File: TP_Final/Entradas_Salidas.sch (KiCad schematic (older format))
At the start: 89 parts, among them J109 BG2, J110 BG2, J111 BG2, J112 Conector pol. 1x3, J113 BG2, J114 Conector pol. 1x3, J115 Conector pol. 1x3, J116 BG2, J117 BG2, Q108 2N3904, Q109 2N3904, Q110 2N3904, U104 OP07, U105 OP07, U106 OP07, U107 LM7805_TO220, U108 LD1117S33TR_SOT223

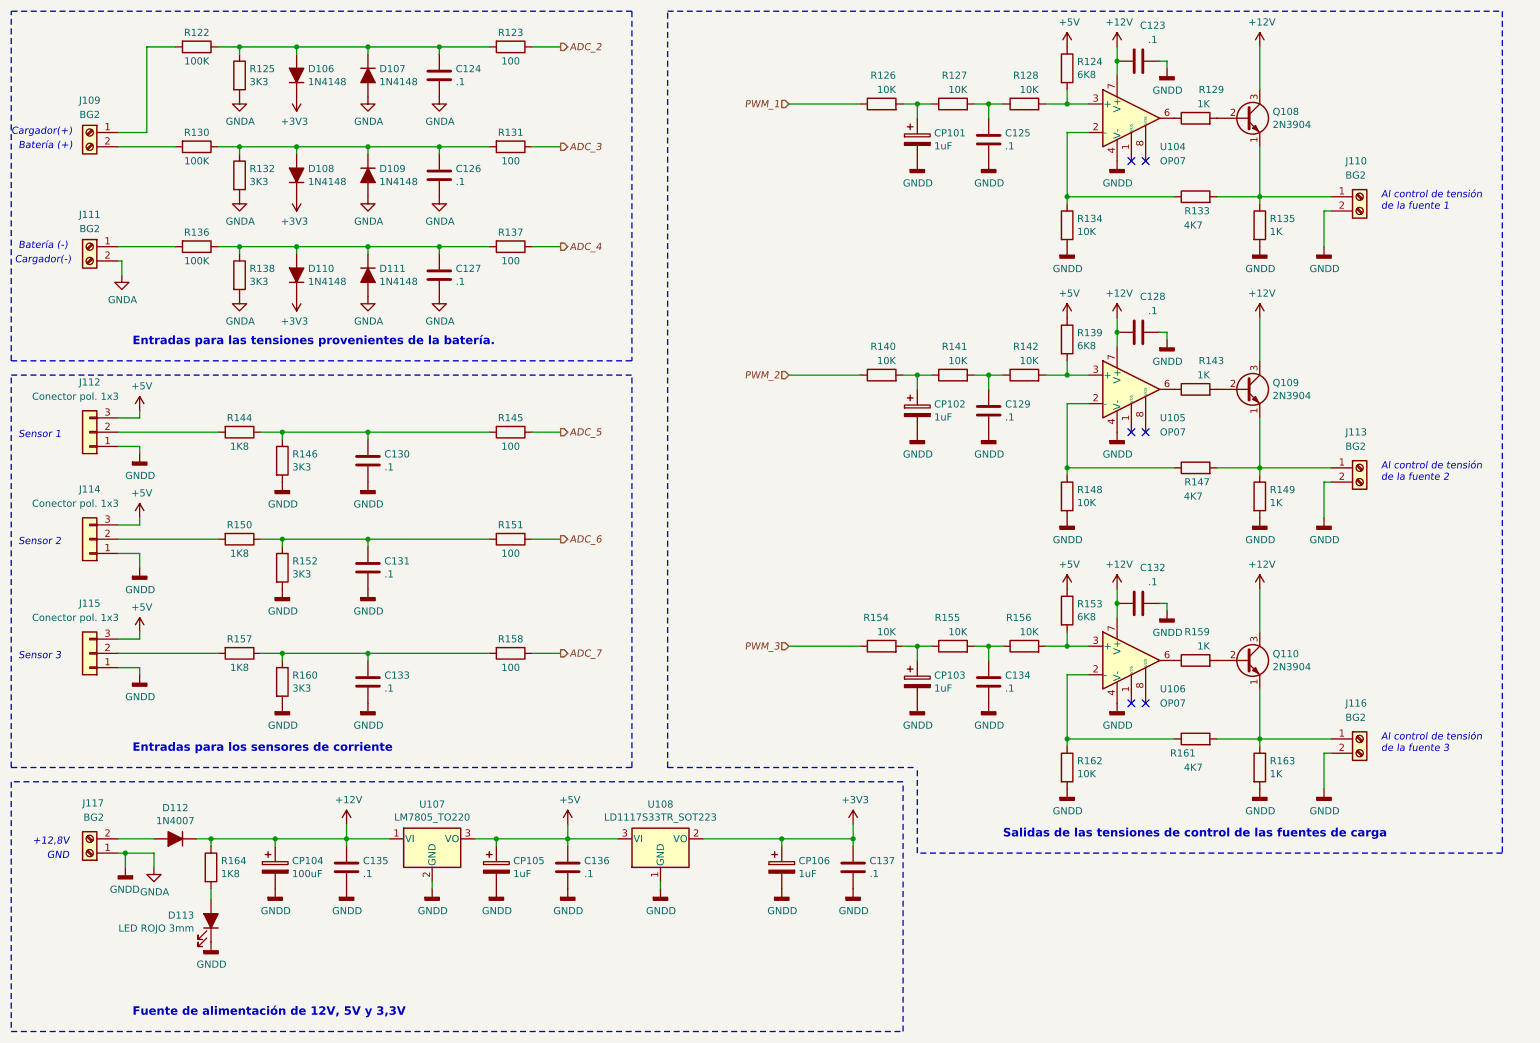
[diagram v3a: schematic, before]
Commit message: Agrego agujeros de montaje y fiduciales al esquematico
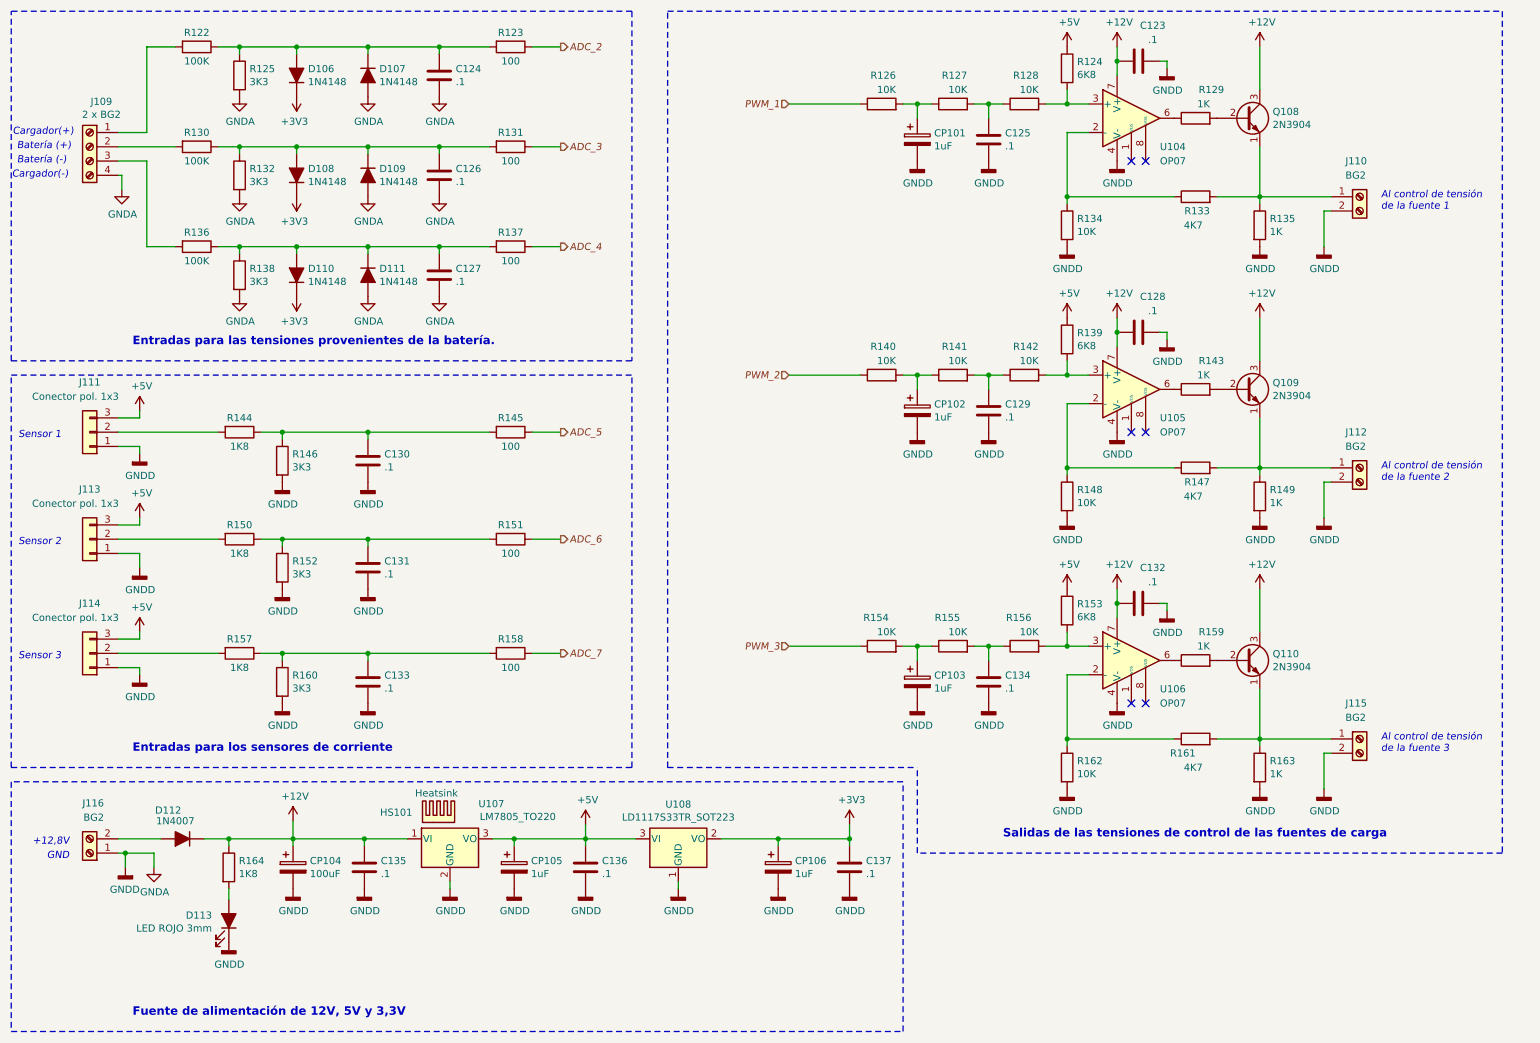
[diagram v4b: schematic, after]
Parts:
- removed J109, J111: BG2, TerminalBlock_Phoenix:TerminalBlock_Phoenix_PT-1,5-2-5.0-H_1x02_P5.00mm_Horizontal, symbol Connector:Screw_Terminal_01x02
- added HS101: Heatsink, Heatsink:Heatsink_Aavid-TV5G_TO220_Horizontal, symbol Mechanical:Heatsink
- added J109: 2 x BG2, TerminalBlock_Phoenix:TerminalBlock_Phoenix_PT-1,5-4-5.0-H_1x04_P5.00mm_Horizontal, symbol Connector:Screw_Terminal_01x04
- renumbered J112 to J111, J113 to J112, J114 to J113, J115 to J114, J116 to J115, J117 to J116
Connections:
- net GNDA: now also J109.4 (Pin_4)
- net at R122.2: now also J109.1 (Pin_1)
- net at R130.2: now also J109.2 (Pin_2)
- net at R136.2: now also J109.3 (Pin_3)
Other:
- moved on the sheet: C135, C136, C137, CP104, CP105, CP106, D112, D113, R164, U107, U108

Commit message: Correccion power flag y digikey part
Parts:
- U106: Digikey part (none) -> OP07DNZ-ND
- U107: Digikey part (none) -> MC7805ACTGOS-ND
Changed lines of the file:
@@
 F 5 "DIP8 - Ultralow Offset Voltage Operational Amplifier" H 8500 5100 50  0001 C CNN "Description"
 F 6 "CI2702050" H 8500 5100 50  0001 C CNN "Elemon part"
+F 7 "OP07DNZ-ND" H 8500 5100 50  0001 C CNN "Digikey part"
 	1    8500 5100
 	1    0    0    -1
@@
 U 1 1 60CF67C7
 P 1200 6450
-F 0 "J116" H 1100 6100 50  0000 L CNN
-F 1 "BG2" H 1100 6200 50  0000 L CNN
+F 0 "J116" H 1175 6100 50  0000 L CNN
+F 1 "BG2" H 1200 6200 50  0000 L CNN
 F 2 "TerminalBlock_Phoenix:TerminalBlock_Phoenix_PT-1,5-2-5.0-H_1x02_P5.00mm_Horizontal" H 1200 6450 50  0001 C CNN
 F 3 "~" H 1200 6450 50  0001 C CNN
@@
 F 5 "1A Fixed Voltage Regulator TO-220" H 3725 6350 50  0001 C CNN "Description"
 F 6 "CI2707457" H 3725 6350 50  0001 C CNN "Elemon part"
+F 7 "MC7805ACTGOS-ND" H 3725 6350 50  0001 C CNN "Digikey part"
 	1    3725 6350
 	1    0    0    -1
@@
 Wire Wire Line
 	2625 6350 3125 6350
+$Comp
+L power:PWR_FLAG #FLG?
+U 1 1 6092C532
+P 2175 6225
+AR Path="/605E6390/6092C532" Ref="#FLG?"  Part="1"
+AR Path="/60564208/6092C532" Ref="#FLG0103"  Part="1"
+F 0 "#FLG0103" H 2175 6300 50  0001 C CNN
+F 1 "PWR_FLAG" H 2175 6398 50  0000 C CNN
+F 2 "" H 2175 6225 50  0001 C CNN
+F 3 "~" H 2175 6225 50  0001 C CNN
+	1    2175 6225
+	1    0    0    -1
+$EndComp
+Wire Wire Line
+	2175 6225 2175 6350
+$Comp
+L power:PWR_FLAG #FLG?
+U 1 1 6093E296
+P 1450 6225
+AR Path="/605E6390/6093E296" Ref="#FLG?"  Part="1"
+AR Path="/60564208/6093E296" Ref="#FLG0104"  Part="1"
+F 0 "#FLG0104" H 1450 6300 50  0001 C CNN
+F 1 "PWR_FLAG" H 1450 6398 50  0000 C CNN
+F 2 "" H 1450 6225 50  0001 C CNN
+F 3 "~" H 1450 6225 50  0001 C CNN
+	1    1450 6225
+	1    0    0    -1
+$EndComp
+Wire Wire Line
+	1450 6450 1450 6225
 $EndSCHEMATC
